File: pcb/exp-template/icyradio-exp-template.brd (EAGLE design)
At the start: 85.7 x 98.4 mm, 3 parts

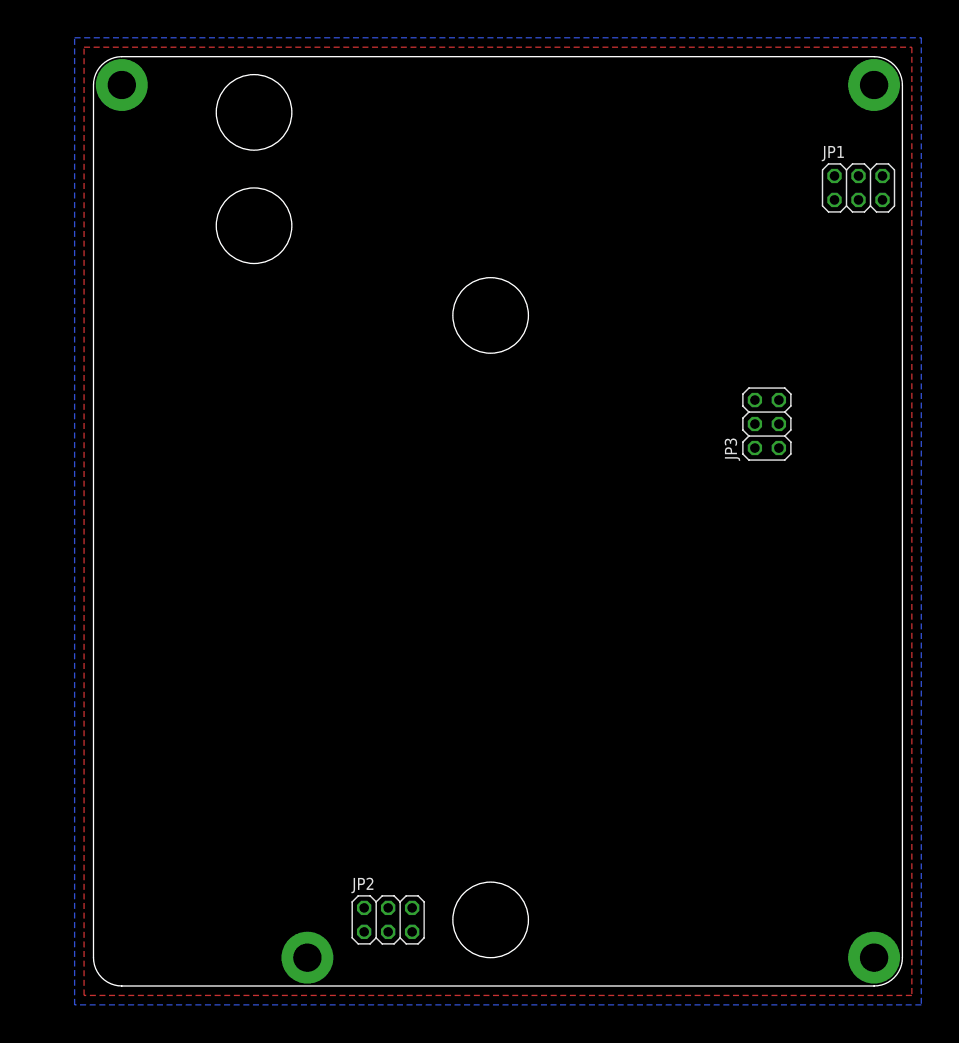
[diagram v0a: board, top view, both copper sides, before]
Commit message: Add expansion board PCB template
Signed-off-by: João Silva <jgc3silva@gmail.com>
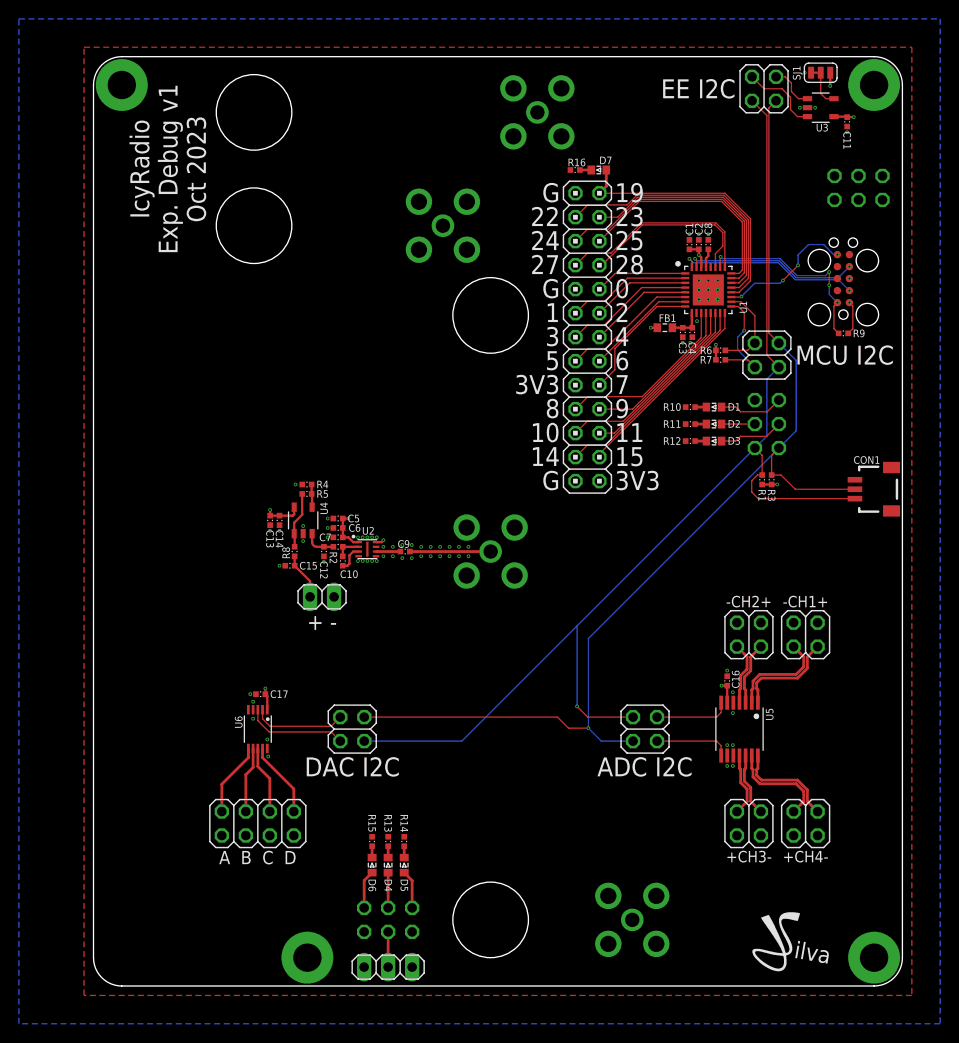
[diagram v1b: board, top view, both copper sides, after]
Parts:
- added C1, C11, C13, C16, C17, C4, C7: 100nF, Capacitor:CAP0402
- added C10: 10nF, Capacitor:CAP0402
- added C12, C14, C5, C6, C8: 1uF, Capacitor:CAP0402
- added C15: DNP, Capacitor:CAP0402
- added C2, C3: 10uF, Capacitor:CAP0402
- added C9: 18pF, Capacitor:CAP0402
- added CON1: 3P-SH-SIDE, JST:SH-03-SIDE
- added D1, D2, D3, D4, D5, D6, D7: LED0603, LED:0603
- added FB1: 1uH, Inductor:IND0603
- added JP10: PINHD-1X2, Pin Header:1X02
- added JP11: PINHD-2X4, Pin Header:2X04
- added JP12, JP13, JP14, JP15, JP6, JP7, JP8, JP9: PINHD-2X2, Pin Header:2X02
- added JP4, JP5: PINHD-2X3, Pin Header:2X03
- added LOGO1: JSILVA-5MM, Silkscreen:JSILVA_5MM
- added R1, R3, R6, R7: 4.7K Ohms, Resistor:RES0402
- added R10, R11, R12, R13, R14, R15, R16: 1K Ohms, Resistor:RES0402
- added R2, R4, R5, R8: 0 Ohms, Resistor:RES0402
- added R9: 10K Ohms, Resistor:RES0402
- added RFCON1, RFCON2, RFCON3, RFCON4: RFCON-SMA, RF Connector:SMA
- added SJ1: (no value), Solder Jumper:SJ2C_S
- added TC1: TC2050-IDC, TagConnect:TC2050-IDC
- added U1: ATSAMD20E16A-M, Microchip:QFN32
- added U2: LTC5597, Analog Devices:DFN8_2X2
- added U3: 24AA02XX-X/OT, Microchip:SOT23-5
- added U4: MCP6V31, Microchip:SOT23-5
- added U5: MCP3424, Microchip:TSSOP14
- added U6: MCP4728-A0, Microchip:MSOP10
- JP1: value PINHD-2X3 -> PINHD-2X13; device Pin Header:2X03 -> Pin Header:2X13
- JP3: value PINHD-2X3 -> PINHD-1X3; device Pin Header:2X03 -> Pin Header:1X03
- moved JP3 70.1 mm to (31.2, 2.00), turned to 0 degrees
- moved JP2 66.1 mm to (71.3, 59.5), flipped to the bottom, turned to 90 degrees
- moved JP1 32.8 mm to (52.3, 68.7), turned to 90 degrees
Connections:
- new net !MCU_RESET: R9.1, TC1.10, U1.26
- new net ADC_C1_N: JP14.4, U5.2
- new net ADC_C1_P: JP14.2, U5.1
- new net ADC_C2_N: JP12.4, U5.4
- new net ADC_C2_P: JP12.2, U5.3
- new net ADC_C3_N: JP15.4, U5.12
- new net ADC_C3_P: JP15.2, U5.11
- new net ADC_C4_N: JP13.4, U5.14
- new net ADC_C4_P: JP13.2, U5.13
- new net ADC_I2C_SCL: JP6.4, U5.8
- new net ADC_I2C_SDA: JP6.2, U5.7
- new net DAC_I2C_SCL: JP7.4, U6.2
- new net DAC_I2C_SDA: JP7.2, U6.3
- new net DAC_VA: JP11.2, U6.6
- new net DAC_VB: JP11.4, U6.7
- new net DAC_VC: JP11.6, U6.8
- new net DAC_VD: JP11.8, U6.9
- new net EE_I2C_SCL: JP8.4, U3.1
- new net EE_I2C_SDA: JP8.2, U3.3
- new net EE_WP: SJ1.2, U3.5
- new net MCU_I2C_SCL: JP9.4, R6.1, U1.18
- new net MCU_I2C_SDA: JP9.2, R7.1, U1.17
- new net MCU_SWCLK: TC1.4, U1.31
- new net MCU_SWDIO: TC1.2, U1.32
- new net MCU_SWO: TC1.6, U1.19
- new net MCU_VDDANA: C3.1, C4.1, FB1.2, U1.9
- new net N$1: C8.1, U1.29
- new net N$14: R5.1, R8.2, U4.1
- new net N$15: C10.2, U2.3
- new net N$16: C10.1, R2.2, U2.2
- new net N$17: C12.1, R2.1, U4.3
- new net N$18: R4.2, R5.2, U4.4
- new net N$19: C9.1, RFCON4.SIGNAL
- new net N$2: D1.C, R10.2
- new net N$20: C9.2, U2.6
- new net N$21: C15.1, JP10.1, R8.1
- new net N$3: D2.C, R11.2
- new net N$4: D3.C, R12.2
- new net N$5: D4.C, R13.2
- new net N$6: D5.C, R14.2
- new net N$7: D6.C, R15.2
- new net N$8: D7.C, R16.2
- new net P0: JP1.17, U1.1
- new net P1: JP1.16, U1.2
- new net P10: JP1.6, U1.13
- new net P11: JP1.5, U1.14
- new net P14: JP1.4, U1.15
- new net P15: JP1.3, U1.16
- new net P19: D7.A, JP1.25, U1.20
- new net P2: JP1.15, U1.3
- new net P22: JP1.24, U1.21
- new net P23: JP1.23, U1.22
- new net P24: JP1.22, U1.23
- new net P25: JP1.21, U1.24
- new net P27: JP1.20, U1.25
- new net P28: JP1.19, U1.27
- new net P3: JP1.14, U1.4
- new net P4: JP1.13, U1.5
- new net P5: JP1.12, U1.6
- new net P6: JP1.11, U1.7
- new net P7: JP1.9, U1.8
- new net P8: JP1.8, U1.11
- new net P9: JP1.7, U1.12
- net 2V5: now also JP4.2; no longer JP1.6
- net 3V3: now also C1.1, C11.1, C13.1, C14.1, C16.1, C17.1, C2.1, C5.1, C6.1, C7.1, FB1.1, JP1.1, JP1.10, JP4.1, R1.2, R3.2, R6.2, R7.2, R9.2, SJ1.3, TC1.1, U1.30, U2.1, U2.8, U3.4, U4.5, U5.6, U6.1; no longer JP1.5
- net 5V0: now also JP4.5, JP4.6; no longer JP1.1, JP1.2
- net EXT_CLK_2_3: now also JP3.2, JP5.3; no longer JP2.3
- net EXT_IO_1_1: now also CON1.2, JP2.2, JP6.3, JP7.3, JP8.3, JP9.3, R3.1; no longer JP3.1
- net EXT_IO_1_2: now also CON1.1, JP2.1, JP6.1, JP7.1, JP8.1, JP9.1, R1.1; no longer JP3.2
- net EXT_IO_1_3: now also D3.A, JP2.4; no longer JP3.3
- net EXT_IO_1_4: now also D2.A, JP2.3; no longer JP3.4
- net EXT_IO_1_5: now also D1.A, JP2.6; no longer JP3.5
- net EXT_IO_2_2: now also D6.A, JP5.6; no longer JP2.2
- net EXT_IO_2_4: now also D4.A, JP5.4; no longer JP2.4
- net EXT_IO_2_6: now also D5.A, JP5.2; no longer JP2.6
- net GND: now also C1.2, C11.2, C12.2, C13.2, C14.2, C15.2, C16.2, C17.2, C2.2, C3.2, C4.2, C5.2, C6.2, C7.2, C8.2, CON1.3, JP1.18, JP1.2, JP1.26, JP10.2, JP11.1, JP11.3, JP11.5, JP11.7, JP12.1, JP12.3, JP13.1, JP13.3, JP14.1, JP14.3, JP15.1, JP15.3, JP3.1, JP3.3, JP4.3, JP4.4, JP5.1, JP5.5, R10.1, R11.1, R12.1, R13.1, R14.1, R15.1, R16.1, R4.1, RFCON4.GND@0, RFCON4.GND@1, RFCON4.GND@2, RFCON4.GND@3, SJ1.1, TC1.3, U1.10, U1.28, U1.33, U2.4, U2.5, U2.7, U2.9, U3.2, U4.2, U5.10, U5.5, U5.9, U6.10, U6.4; no longer JP1.3, JP1.4, JP2.1, JP3.6
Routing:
- net EXT_IO_1_2: track 0.00 -> 125.1 mm, vias 0 -> 1
- net EXT_IO_1_1: track 0.00 -> 119.2 mm, vias 0 -> 1
- net P19: track 0.00 -> 29.0 mm
- net P22: track 0.00 -> 28.8 mm
- net 3V3: track 0.00 -> 28.0 mm, vias 0 -> 12
- net P24: track 0.00 -> 27.8 mm
- net P23: track 0.00 -> 25.2 mm
- net P25: track 0.00 -> 24.2 mm
- net P14: track 0.00 -> 22.7 mm
- net P27: track 0.00 -> 21.8 mm
- net P10: track 0.00 -> 20.9 mm
- net !MCU_RESET: track 0.00 -> 20.8 mm, vias 0 -> 4
- net P15: track 0.00 -> 20.8 mm
- net MCU_SWDIO: track 0.00 -> 19.3 mm, vias 0 -> 2
- net P28: track 0.00 -> 19.1 mm
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- added copper zone on layer 15, net 3V3
- added copper zone on layer 15, net GND
- added copper zone on layer 2, net GND
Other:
- board text added: "+ -"
- board text added: "+CH3-"
- board text added: "+CH4-"
- board text added: "-CH1+"
- board text added: "-CH2+"
- board text added: "0"
- board text added: "1"
- board text added: "10"
- board text added: "11"
- board text added: "14"
- board text added: "15"
- board text added: "19"
- board text added: "2"
- board text added: "22"
- board text added: "23"
- board text added: "24"
- board text added: "25"
- board text added: "27"
- board text added: "28"
- board text added: "3"
- board text added: "3V3"
- board text added: "4"
- board text added: "5"
- board text added: "6"
- board text added: "7"
- board text added: "8"
- board text added: "9"
- board text added: "A B C D"
- board text added: "ADC I2C"
- board text added: "DAC I2C"
- board text added: "EE I2C"
- board text added: "G"
- board text added: "IcyRadio Exp. Debug v1 Oct 2023"
- board text added: "MCU I2C"
